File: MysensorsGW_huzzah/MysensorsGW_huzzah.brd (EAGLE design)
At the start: 29.2 x 27 mm, 7 parts

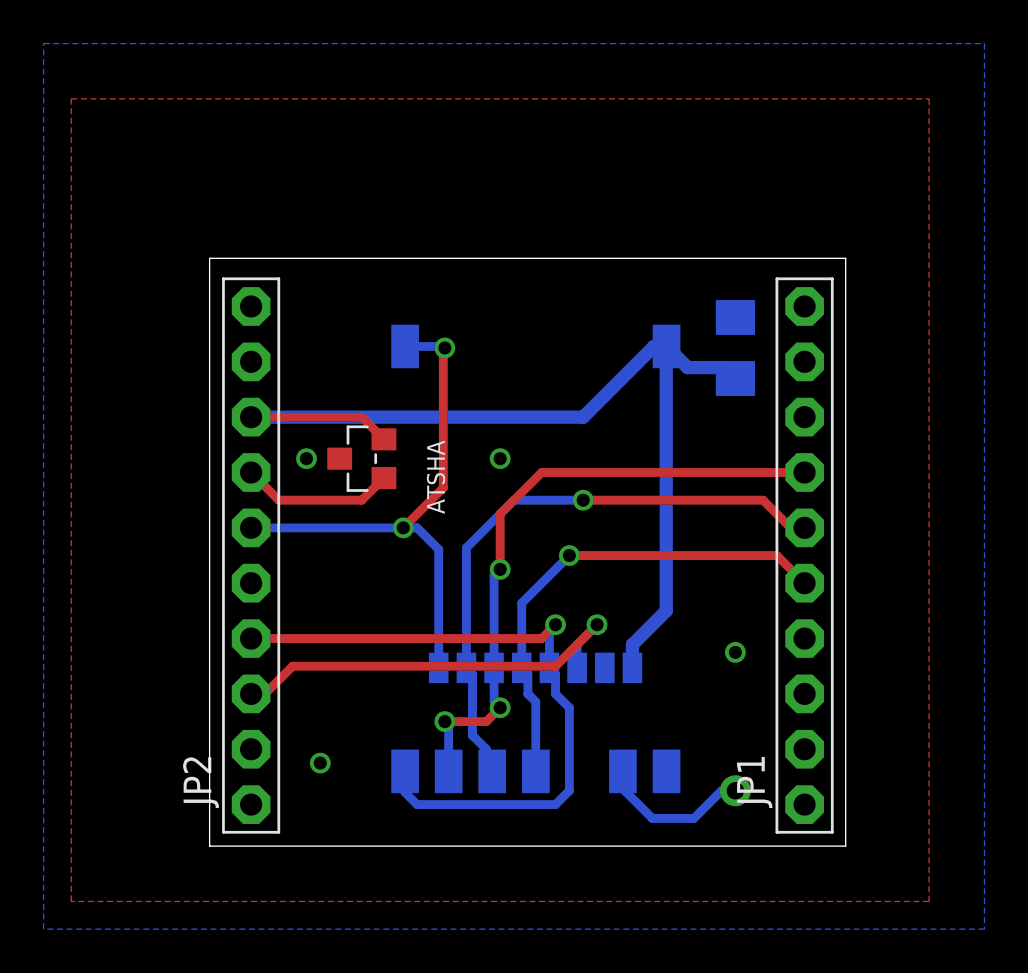
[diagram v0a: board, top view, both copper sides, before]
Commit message: gnd plane under nrf removed
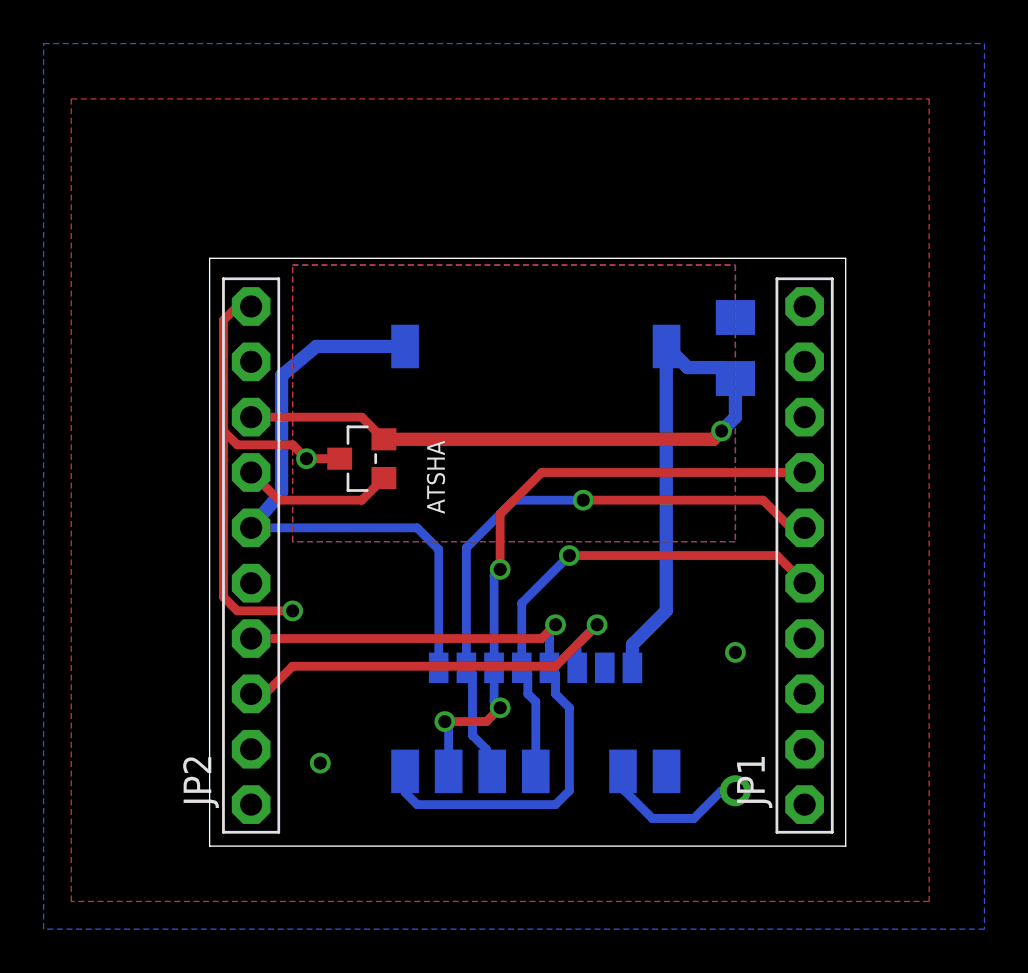
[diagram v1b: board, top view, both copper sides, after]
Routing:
- net GND: track 0.00 -> 23.5 mm
- net D2: track 25.4 -> 28.1 mm, vias 2 -> 0
- net VCC3OUT: track 45.9 -> 43.8 mm, vias 0 -> 1
- added copper zone on layer 1, net N$2
- added copper zone on layer 16, net N$3
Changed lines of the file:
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@@
 <setting verticaltext="up"/>
 </settings>
-<grid distance="0.05" unitdist="inch" unit="mil" style="lines" multiple="1" display="yes" altdistance="0.025" altunitdist="inch" altunit="mil"/>
+<grid distance="0.05" unitdist="inch" unit="mil" style="lines" multiple="1" display="yes" altdistance="10" altunitdist="mil" altunit="mil"/>
 <layers>
 <layer number="1" name="Top" color="4" fill="1" visible="yes" active="yes"/>
@@
 <wire x1="0" y1="26.975" x2="0" y2="0" width="0" layer="20"/>
 <text x="24.765" y="6.35" size="0.8128" layer="22" rot="MR270">ANT</text>
-<dimension x1="29.19" y1="26.975" x2="0" y2="26.975" x3="14.595" y3="27.94" textsize="1.778" layer="20"/>
-<dimension x1="0" y1="26.975" x2="0" y2="0" x3="-1.27" y3="13.4875" textsize="1.778" layer="20"/>
 </plain>
 <attributes>
@@
 <via x="4.445" y="17.78" extent="1-16" drill="0.6"/>
 <via x="5.08" y="3.81" extent="1-16" drill="0.6"/>
-<via x="13.335" y="17.78" extent="1-16" drill="0.6"/>
+<via x="3.81" y="10.795" extent="1-16" drill="0.6"/>
+<wire x1="1.905" y1="24.765" x2="1.27" y2="24.765" width="0.4064" layer="1"/>
+<wire x1="1.27" y1="24.765" x2="0.635" y2="24.13" width="0.4064" layer="1"/>
+<wire x1="0.635" y1="24.13" x2="0.635" y2="19.05" width="0.4064" layer="1"/>
+<wire x1="0.635" y1="19.05" x2="1.27" y2="18.415" width="0.4064" layer="1"/>
+<wire x1="1.27" y1="18.415" x2="3.81" y2="18.415" width="0.4064" layer="1"/>
+<wire x1="3.81" y1="18.415" x2="4.445" y2="17.78" width="0.4064" layer="1"/>
+<wire x1="5.969" y1="17.78" x2="4.445" y2="17.78" width="0.4064" layer="1"/>
+<wire x1="3.81" y1="10.795" x2="1.27" y2="10.795" width="0.4064" layer="1"/>
+<wire x1="1.27" y1="10.795" x2="0.635" y2="11.43" width="0.4064" layer="1"/>
+<wire x1="0.635" y1="11.43" x2="0.635" y2="19.05" width="0.4064" layer="1"/>
 </signal>
 <signal name="VIN">
@@
 <wire x1="10.515" y1="8.18" x2="10.515" y2="13.615" width="0.4064" layer="16"/>
 <wire x1="10.515" y1="13.615" x2="9.525" y2="14.605" width="0.4064" layer="16"/>
-<wire x1="9.525" y1="14.605" x2="8.89" y2="14.605" width="0.4064" layer="16"/>
-<via x="8.89" y="14.605" extent="1-16" drill="0.6" shape="square"/>
-<wire x1="8.89" y1="14.605" x2="1.905" y2="14.605" width="0.4064" layer="16"/>
-<wire x1="10.725" y1="16.44" x2="8.89" y2="14.605" width="0.4064" layer="1"/>
-<wire x1="10.725" y1="16.44" x2="10.725" y2="22.79" width="0.4064" layer="1"/>
-<wire x1="10.725" y1="22.79" x2="10.795" y2="22.86" width="0.4064" layer="1"/>
-<via x="10.795" y="22.86" extent="1-16" drill="0.6" shape="square"/>
-<wire x1="8.97" y1="22.93" x2="10.725" y2="22.93" width="0.4064" layer="16"/>
-<wire x1="10.725" y1="22.93" x2="10.795" y2="22.86" width="0.4064" layer="16"/>
+<wire x1="9.525" y1="14.605" x2="1.905" y2="14.605" width="0.4064" layer="16"/>
+<wire x1="8.97" y1="22.93" x2="4.896" y2="22.93" width="0.6096" layer="16"/>
+<wire x1="4.896" y1="22.93" x2="3.302" y2="21.59" width="0.6096" layer="16"/>
+<wire x1="3.302" y1="21.59" x2="3.302" y2="16.256" width="0.6096" layer="16"/>
+<wire x1="3.302" y1="16.256" x2="1.905" y2="14.605" width="0.6096" layer="16"/>
 </signal>
 <signal name="D4">
@@
 <wire x1="20.955" y1="22.225" x2="21.315" y2="22.585" width="0.4064" layer="16"/>
 <wire x1="23.63" y1="21.96" x2="24.13" y2="21.46" width="0.4064" layer="16"/>
-<wire x1="20.97" y1="22.93" x2="20.39" y2="22.93" width="0.6096" layer="16"/>
-<wire x1="20.39" y1="22.93" x2="17.145" y2="19.685" width="0.6096" layer="16"/>
-<wire x1="17.145" y1="19.685" x2="1.905" y2="19.685" width="0.6096" layer="16"/>
 <wire x1="19.405" y1="8.61" x2="19.405" y2="9.245" width="0.6096" layer="16"/>
 <wire x1="19.405" y1="9.245" x2="20.955" y2="10.795" width="0.6096" layer="16"/>
@@
 <wire x1="8.001" y1="18.669" x2="6.985" y2="19.685" width="0.4064" layer="1"/>
 <wire x1="6.985" y1="19.685" x2="1.905" y2="19.685" width="0.4064" layer="1"/>
+<wire x1="8.001" y1="18.669" x2="23.114" y2="18.669" width="0.6096" layer="1"/>
+<wire x1="23.114" y1="18.669" x2="23.495" y2="19.05" width="0.6096" layer="1"/>
+<via x="23.495" y="19.05" extent="1-16" drill="0.6" shape="square"/>
+<wire x1="24.13" y1="21.46" x2="24.13" y2="19.685" width="0.6096" layer="16"/>
+<wire x1="24.13" y1="19.685" x2="23.495" y2="19.05" width="0.6096" layer="16"/>
 </signal>
 <signal name="N$1">
@@
 <wire x1="19.05" y1="3.35" x2="18.97" y2="3.43" width="0.4064" layer="16"/>
 </signal>
+<signal name="N$2">
+<polygon width="0" layer="1" pour="cutout">
+<vertex x="3.81" y="26.67"/>
+<vertex x="24.13" y="26.67"/>
+<vertex x="24.13" y="13.97"/>
+<vertex x="3.81" y="13.97"/>
+</polygon>
+</signal>
+<signal name="N$3">
+<polygon width="0" layer="16" pour="cutout">
+<vertex x="3.81" y="26.67"/>
+<vertex x="24.13" y="26.67"/>
+<vertex x="24.13" y="13.97"/>
+<vertex x="3.81" y="13.97"/>
+</polygon>
+</signal>
 </signals>
